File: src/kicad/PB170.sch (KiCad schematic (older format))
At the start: 33 parts, among them J1 USB_C_Receptacle_USB2.0-Conne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, J2 USB_B_Micro, Q1 P-MOSFET-MLP_HS, Q2 BC817, SW1 SW_MEC_5E, SW2 SW_MEC_5E

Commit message: First KiCad trials
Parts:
- removed C4: 10uF, Capacitors_SMD:C_0805, symbol Device:C
- removed D3: LED yellow, LEDs:LED_0603, symbol Device:LED
- removed J1: USB_C_Receptacle_USB2.0-Connector, PB170:USB_C_Female-16Pin-HPJF, symbol PB170:USB_C_Receptacle_USB2.0-Connector
- removed R10, R12: 220R, Resistors_SMD:R_0603, symbol Device:R
- removed R3: 180R, Resistors_SMD:R_0603, symbol Device:R
- removed R5: 10k, Resistors_SMD:R_0603, symbol Device:R
- removed SW2: SW_MEC_5E, PB170:TactileSwitch_C381064, symbol Switch:SW_MEC_5E
- added D? (x3): LED green, LEDs:LED_0603, symbol Device:LED
- added D? (x3): LED white, LEDs:LED_0603, symbol Device:LED
- added D? (x3): LED blue, LEDs:LED_0603, symbol Device:LED
- added Q? (x3): BC817, TO_SOT_Packages_SMD:SOT-23, symbol Transistor_BJT:BC817
- added R? (x3): 180R, Resistors_SMD:R_0603, symbol Device:R
- added R? (x3): 130R, Resistors_SMD:R_0603, symbol Device:R
- added R? (x3): 220R, Resistors_SMD:R_0603, symbol Device:R
- added U? (x2): 74LS73, symbol 74xx:74LS73
- added U? (x2): 74LVC1GU04DRL, Package_TO_SOT_SMD:SOT-553, symbol 74xGxx:74LVC1GU04DRL
- added U? (x2): 74AUC1G74, symbol 74xGxx:74AUC1G74
- added U?: 74LVC2G32, symbol 74xGxx:74LVC2G32
- added U? (x2): 74HC08, Housings_SOIC:SOIC-14_3.9x8.7mm_Pitch1.27mm, symbol PB170:74HC08
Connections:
- net labels removed: OUTPUT
- wire segments 66 -> 99
- no-connect marks 9 -> 5
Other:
- note removed: "USB supply"
- note removed: "XOR using 4 NANDs"
- moved on the sheet: C3, D2, D4, D5, D6, H1, H2, H3, H4, J2, Q2, R11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

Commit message: added basic circuit layout
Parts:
- removed C1: 10uF, Capacitors_SMD:C_0805, symbol Device:C
- removed C2: 100nF, Capacitors_SMD:C_0603, symbol Device:C
- removed D1: LED red, LEDs:LED_0603, symbol Device:LED
- removed J_PWR1: Conn_01x03, Pin_Headers:Pin_Header_Straight_1x03_Pitch2.54mm, symbol Connector_Generic:Conn_01x03
- removed Q1: P-MOSFET-MLP_HS, PB170:MLP3.3X3.3_HS, symbol PB170:P-MOSFET-MLP_HS
- removed R1: 220R, Resistors_SMD:R_0603, symbol Device:R
- removed R9: 10k, Resistors_SMD:R_0603, symbol Device:R
- removed U? (x2): 74LVC1GU04DRL, Package_TO_SOT_SMD:SOT-553, symbol 74xGxx:74LVC1GU04DRL
- added U1, U13, U14, U15, U16, U17, U18, U19, U20, U6: 74AHC1G32, symbol 74xGxx:74AHC1G32
- gave numbers to parts that had none: 27
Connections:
- net labels removed: +5V
- wire segments 99 -> 104
- no-connect marks 5 -> 27
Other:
- note added: "clock signal"
- note added: "const 1\n"
- note removed: "Power management"
- moved on the sheet: D1, D2, D3, D4, D5, D6, D7, H1, H2, H3, H4, J2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

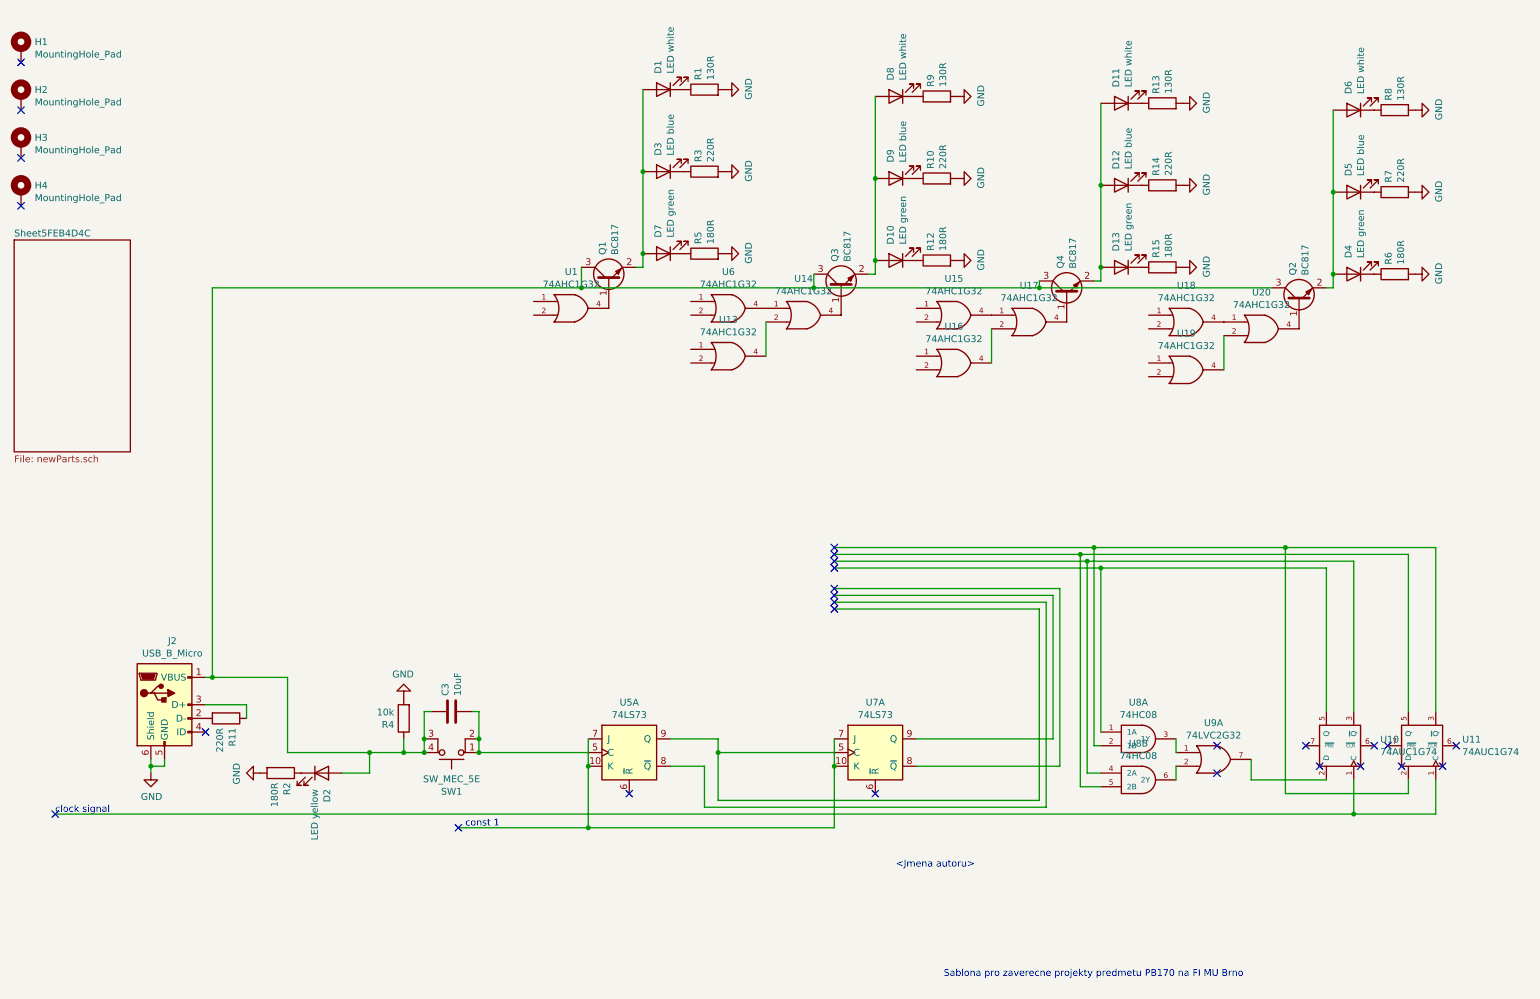
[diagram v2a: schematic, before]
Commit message: Changed logical OR components
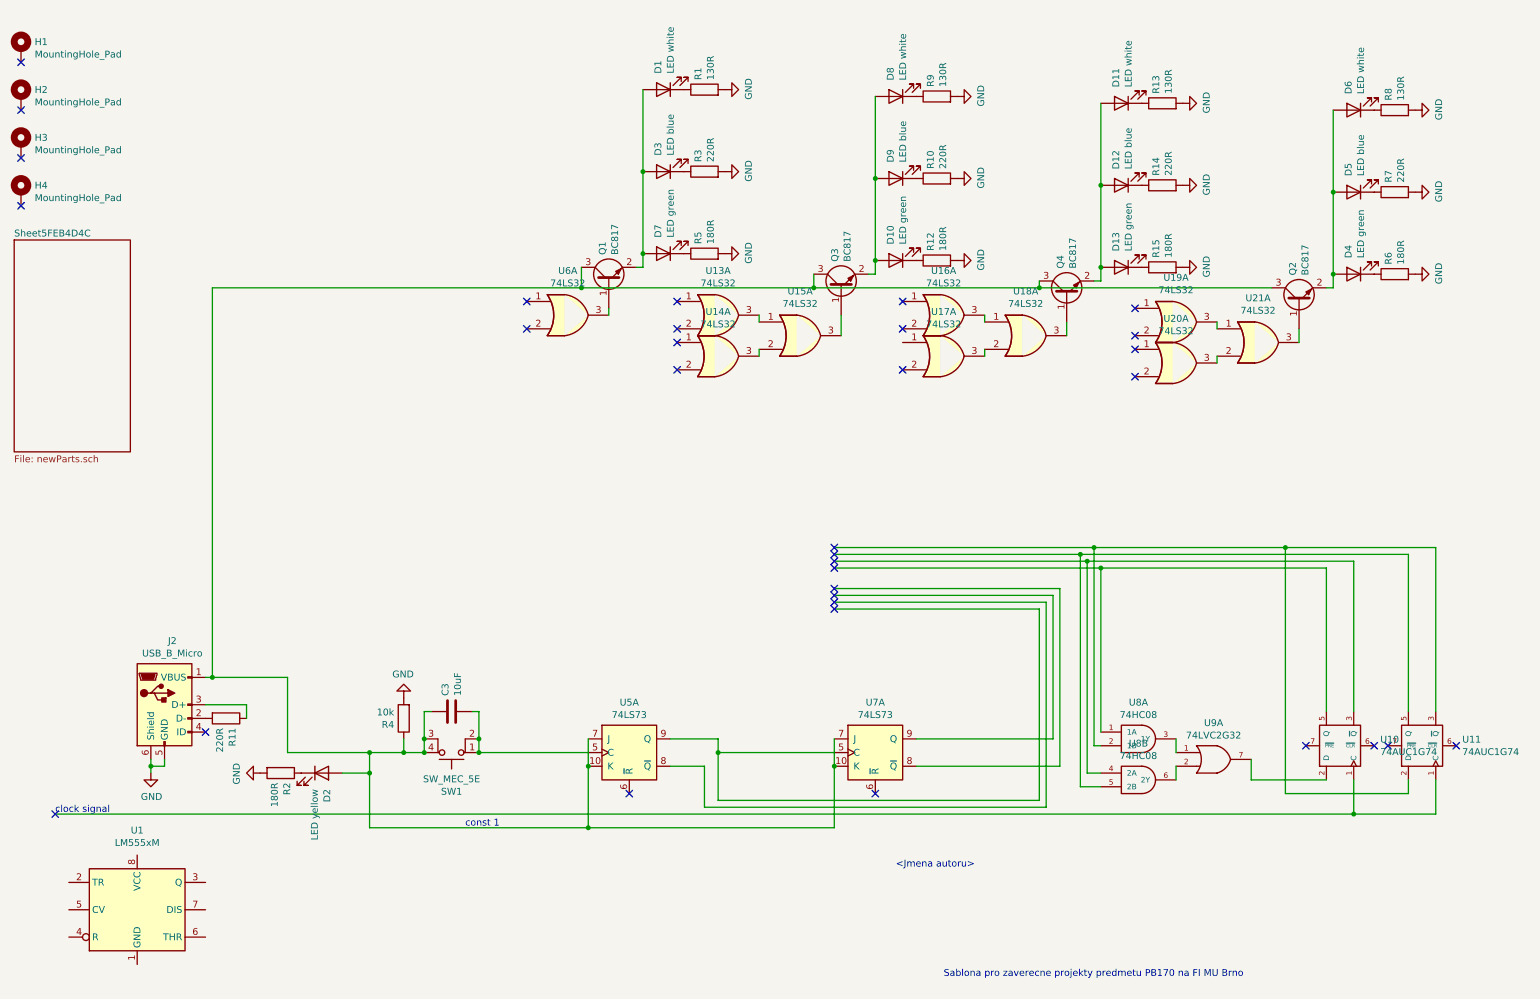
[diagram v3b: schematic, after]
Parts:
- removed U1, U13, U14, U15, U16, U17, U18, U19, U20, U6: 74AHC1G32, symbol 74xGxx:74AHC1G32
- added U1: LM555xM, Package_SO:SOIC-8_3.9x4.9mm_P1.27mm, symbol Timer:LM555xM
- added U13, U14, U15, U16, U17, U18, U19, U20, U21, U6: 74LS32, symbol 74xx:74LS32
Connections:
- net at C3.1, D2.2 (A), J2.1 (VBUS)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: now also U5.10 (K), U5.7 (J), U7.10 (K), U7.7 (J)
- net at Q2.1 (B): now also U21.3
- net at Q4.1 (B): now also U18.3
- net at Q3.1 (B): now also U15.3
- net at Q1.1 (B): now also U6.3
- new net: U13.3, U15.1
- new net: U14.3, U15.2
- new net: U16.3, U18.1
- new net: U17.3, U18.2
- new net: U19.3, U21.1
- new net: U20.3, U21.2
- no-connect marks 27 -> 33
